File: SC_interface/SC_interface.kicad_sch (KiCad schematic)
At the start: 0 parts

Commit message: updated desgin doc, draw draft of the schematic
V1 circuit
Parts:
- added C1, C12: 0.47uf 400V, symbol Device:C_Small
- added C10, C11, C2, C5, C7: 0.1uf, symbol Device:C_Small
- added C3, C4, C6, C8, C9: 330uf 25V, symbol Device:C_Polarized_Small
- added D1: SMCJ6.0A, PCM_Diode_SMD_AKL:D_SMC, symbol PCM_Diode_TVS_AKL:SMCJ6.0A
- added D2, D3, D4, D5: 1N4148W, digikey-footprints:SOD-123, symbol dk_Diodes-Rectifiers-Single:1N4148W-7-F
- added F2: MF-MSMF110, MF-MSMF110:FUSER_MF-MSMF110, symbol MF-MSMF110:MF-MSMF110
- added J1: Input1, PCM_SparkFun-Connector:1x02, symbol Connector:Conn_Coaxial
- added J2: Output_BNC1, PCM_SparkFun-Connector:1x02, symbol Connector:Conn_Coaxial
- added Q1, Q2, Q3, Q4: LND150N8, PCM_Package_TO_SOT_SMD_AKL:SOT-89-3, symbol PCM_Transistor_MOSFET_AKL:LND150N8
- added R1: 90.9k, PCM_SparkFun-Resistor:R_0603_1608Metric, symbol PCM_SparkFun-Resistor:R_Small
- added R2: 9.09k, PCM_SparkFun-Resistor:R_0603_1608Metric, symbol PCM_SparkFun-Resistor:R_Small
- added R3: 909, PCM_SparkFun-Resistor:R_0603_1608Metric, symbol PCM_SparkFun-Resistor:R_Small
- added R4: 102, PCM_SparkFun-Resistor:R_0603_1608Metric, symbol PCM_SparkFun-Resistor:R_Small
- added R5: 100k, PCM_SparkFun-Resistor:R_0603_1608Metric, symbol PCM_SparkFun-Resistor:R_Small
- added SW1: Main Power, Button_Switch_SMD:Nidec_Copal_CAS-120A, symbol Switch:SW_DPDT_x2
- added SW2: SW_Select, PCM_SparkFun-Resistor:R_0603_1608Metric, symbol Switch:SW_Rotary_1x4_MP
- added U1: JCA0305D03, JCA0305D03:XPDCDCCONV, symbol JCA0305D03:JCA0305D03
- added U2: U2 OPA1656IDR, Package_SO:SOIC-8_3.9x4.9mm_P1.27mm, symbol Amplifier_Operational:OPA1656ID
- added U3: INA134UA, PCM_Package_SO_AKL:SO-8_3.9x4.9mm_P1.27mm, symbol PCM_Amplifier_Difference_AKL:INA134UA
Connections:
- new net: Q3.1 (G), Q3.2 (S), Q4.1 (G), Q4.2 (S)
- new net: C12.2, Q3.3 (D), R4.1, R5.2
- new net: Q1.1 (G), Q1.2 (S), Q2.1 (G), Q2.2 (S)
- new net: Q1.3 (D), SW2.5
- new net: C6.1, C7.1, SW1.2 (B), U1.14 (+VOUT)
- new net: R3.1, R4.2, SW2.4
- new net: R2.1, R3.2, SW2.3
- new net: C2.1, C3.1, D1.1 (K), F2.2, U1.22 (+VIN), U1.23 (+VIN2)
- new net: R1.1, R2.2, SW2.2
- new net: C1.2, R1.2, SW2.1
- new net: U2.7, U3.2 (IN-)
- new net: U2.1, U3.3 (IN+)
- new net: J2.1 (In), U3.5 (SENSE), U3.6 (OUT)
- new net: C4.2, C5.1, SW1.5 (B), U1.11 (-VOUT)
- new net: D2.A, D3.K, Q2.3 (D), U2.3 (+)
- new net: C12.1, J1.2 (Ext)
- new net: D4.A, D5.K, Q4.3 (D), U2.5 (+)
- new net: C1.1, J1.1 (In)
- new net +5V: F2.1
- new net +VDC: C11.1, C8.1, D2.K, D4.K, SW1.3 (C), U2.8 (V+), U3.7 (V+)
- new net -VDC: C10.1, C9.2, D3.A, D5.A, SW1.6 (C), U2.4 (V-), U3.4 (V-)
- new net GND: C10.2, C11.2, C4.1, C5.2, C6.2, C7.2, C8.2, C9.1, J2.2 (Ext), R5.1, U1.16 (COMMON2), U1.9 (COMMON), U3.1 (REF)
- new net GNDREF: C2.2, C3.2, D1.2 (A), U1.2 (-VIN), U1.3 (-VIN2)

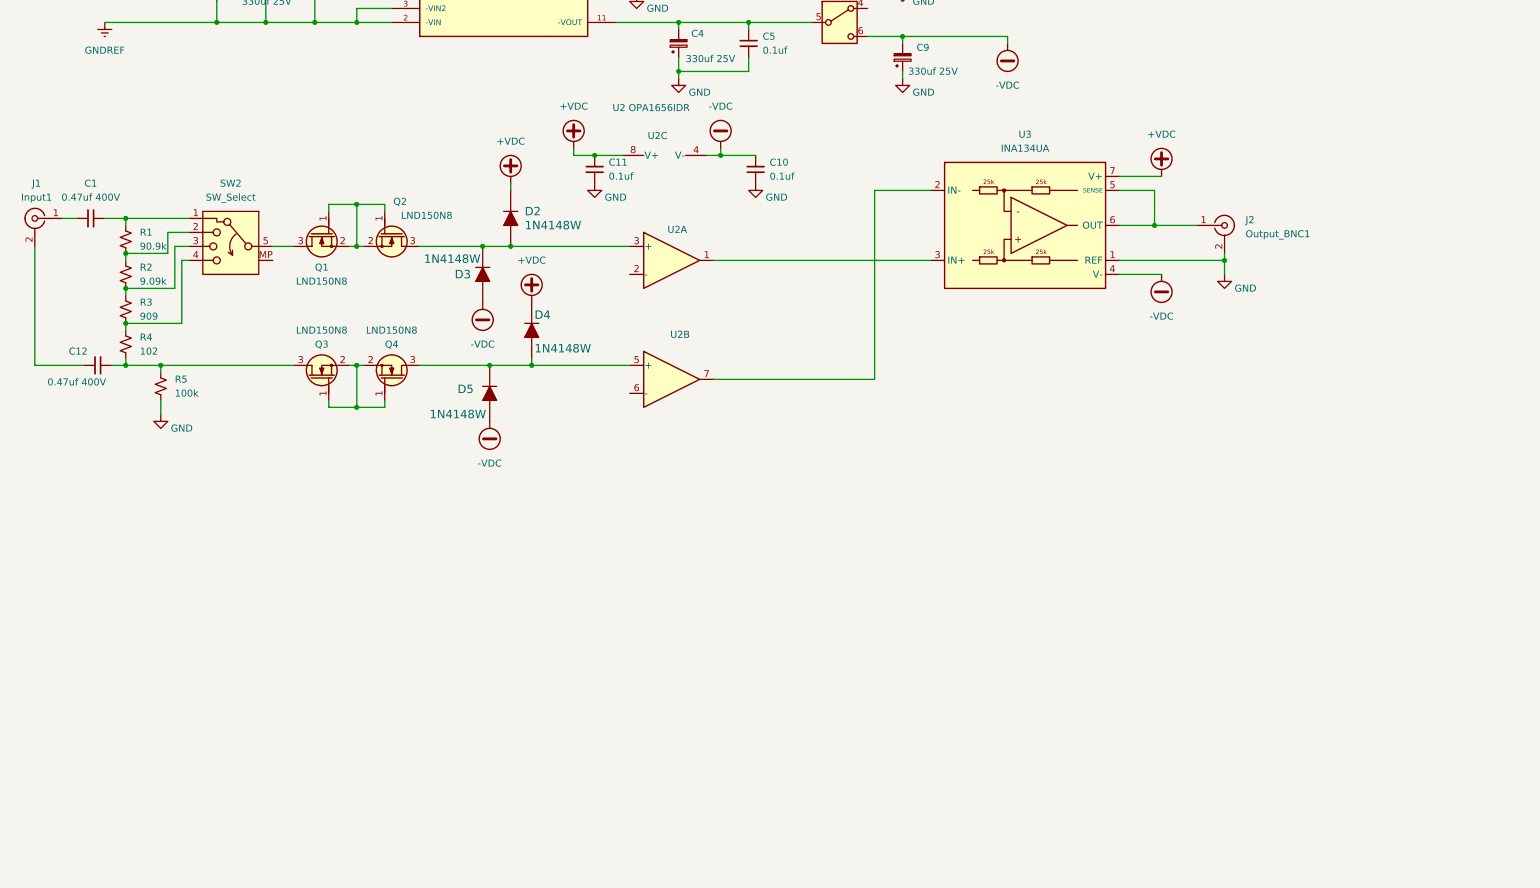
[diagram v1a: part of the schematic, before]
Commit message: completed Channel 1
completed two opamps
completed clamping network
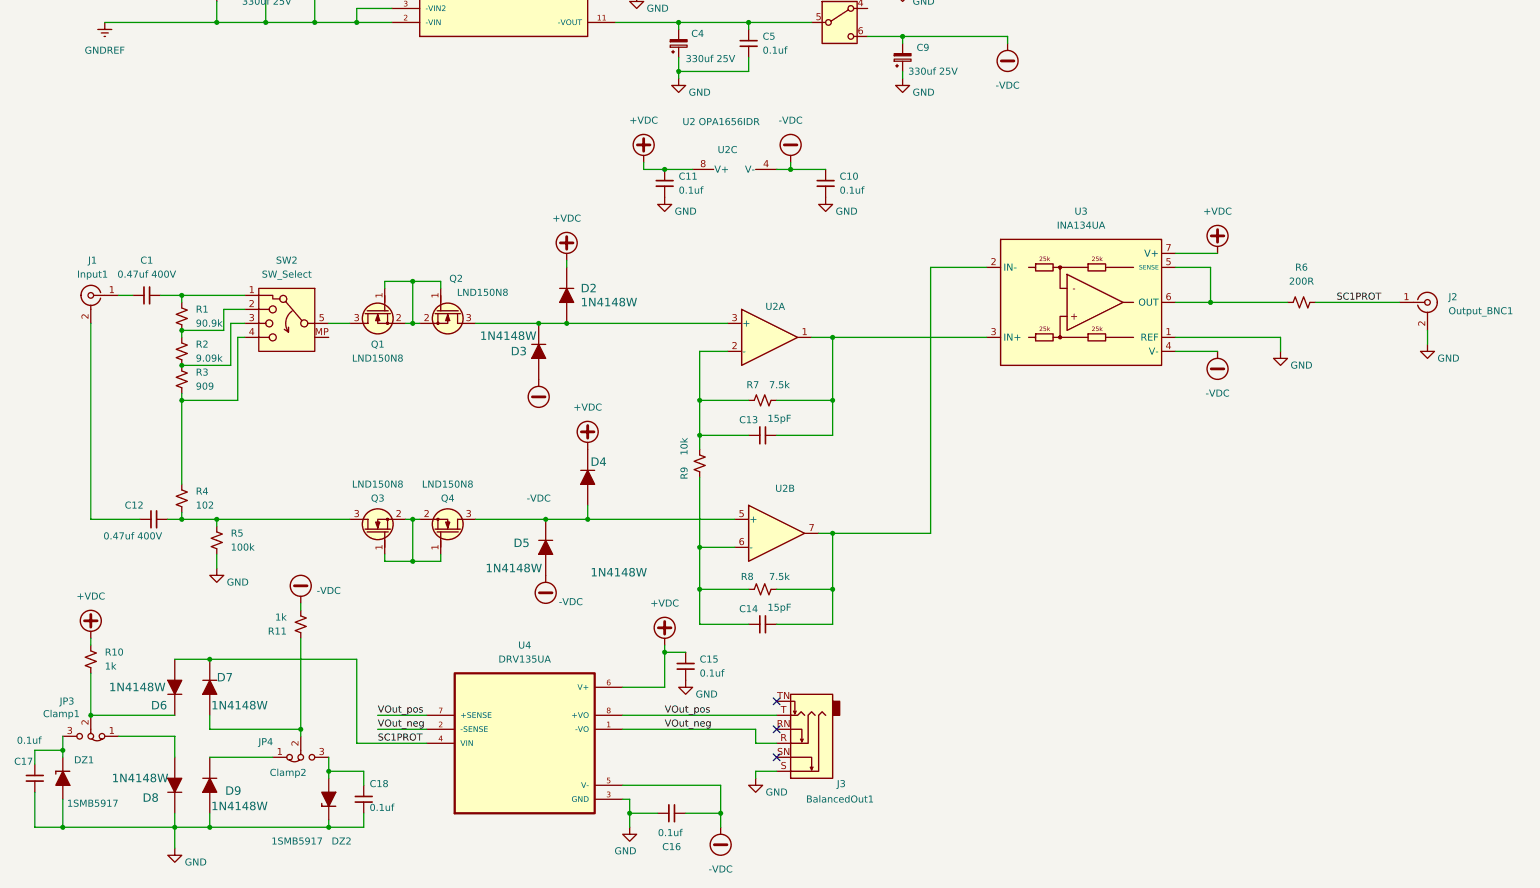
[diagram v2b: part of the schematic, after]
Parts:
- added C13, C14: 15pF, PCM_SparkFun-Resistor:R_0603_1608Metric, symbol Device:C_Small
- added C15, C16, C17, C18: 0.1uf, symbol Device:C_Small
- added D6, D7, D8, D9: 1N4148W, digikey-footprints:SOD-123, symbol dk_Diodes-Rectifiers-Single:1N4148W-7-F
- added DZ1, DZ2: 1SMB5917, PCM_Diode_SMD_AKL:D_SMB, symbol PCM_Diode_Zener_AKL:1SMB5917
- added J3: BalancedOut1, Connector_Audio:Jack_6.35mm_Neutrik_NMJ6HCD2_Horizontal, symbol Connector_Audio:NMJ6HCD2
- added JP3: Clamp1, Package_LCC:PLCC-84_29.3x29.3mm_P1.27mm, symbol Jumper:Jumper_3_Bridged12
- added JP4: Clamp2, Package_LCC:PLCC-84_29.3x29.3mm_P1.27mm, symbol Jumper:Jumper_3_Bridged12
- added R10, R11: 1k, PCM_SparkFun-Resistor:R_0603_1608Metric, symbol PCM_SparkFun-Resistor:R_Small
- added R6: 200R, PCM_SparkFun-Resistor:R_0603_1608Metric, symbol PCM_SparkFun-Resistor:R_Small
- added R7, R8: 7.5k, PCM_SparkFun-Resistor:R_0603_1608Metric, symbol PCM_SparkFun-Resistor:R_Small
- added R9: 10k, PCM_SparkFun-Resistor:R_0603_1608Metric, symbol PCM_SparkFun-Resistor:R_Small
- added U4: DRV135UA, DRV135UA:SOIC127P599X175-8N, symbol DRV135UA:DRV135UA
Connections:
- net +VDC: now also C15.1, R10.2, U4.6 (V+)
- net -VDC: now also C16.2, R11.1, U4.5 (V-)
- net GND: now also C15.2, C16.1, C17.1, C18.1, D8.K, D9.A, DZ1.2 (A), DZ2.1 (K), J3.S, U4.3 (GND)
- net at U2.7, U3.2 (IN-): now also C14.2, R8.2
- net at U2.1, U3.3 (IN+): now also C13.2, R7.2
- net at U3.5 (SENSE), U3.6 (OUT): now also R6.1; no longer J2.1 (In)
- net at U2.2 (-): now also C13.1, R7.1, R9.2
- net at U2.6 (-): now also C14.1, R8.1, R9.1
- new net: D8.A, JP3.1 (A)
- new net: C18.2, DZ2.2 (A), JP4.3 (B)
- new net: D6.K, JP3.2 (C), R10.1
- new net: C17.2, DZ1.1 (K), JP3.3 (B)
- new net: D9.K, JP4.1 (A)
- new net: D7.A, JP4.2 (C), R11.2
- new net SC1PROT: D6.A, D7.K, J2.1 (In), R6.2, U4.4 (VIN)
- new net VOut_neg: J3.R, U4.1 (-VO), U4.2 (-SENSE)
- new net VOut_pos: J3.T, U4.7 (+SENSE), U4.8 (+VO)
- no-connect marks 0 -> 3
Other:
- moved on the sheet: C1, C10, C11, C12, D2, D3, D4, D5, J1, J2, Q1, Q2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

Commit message: added channel 2
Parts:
- SW2: value SW_Select -> SW_Select1
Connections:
- net VOut_neg renamed VOut_neg1
- net VOut_pos renamed VOut_pos1
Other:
- added sheet Channel2 (Channel2.kicad_sch)
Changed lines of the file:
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@@
 		)
 	)
-	(label "VOut_pos"
+	(label "VOut_pos1"
 		(at 80.01 167.64 0)
 		(effects
@@
 		)
 	)
-	(label "VOut_pos"
+	(label "VOut_pos1"
 		(at 132.08 167.64 0)
 		(effects
@@
 		)
 	)
-	(label "VOut_neg"
+	(label "VOut_neg1"
 		(at 132.08 170.18 0)
 		(effects
@@
 		)
 	)
-	(label "VOut_neg"
+	(label "VOut_neg1"
 		(at 80.01 170.18 0)
 		(effects
@@
 			)
 		)
-		(property "Value" "SW_Select"
+		(property "Value" "SW_Select1"
 			(at 63.5 87.63 0)
 			(show_name no)
@@
 		(in_pos_files yes)
 		(dnp no)
-		(fields_autoplaced yes)
 		(property "Reference" "J1"
-			(at 28.2574 85.09 0)
+			(at 23.114 86.868 0)
 			(show_name no)
 			(do_not_autoplace no)
@@
 		)
 		(property "Value" "Input1"
-			(at 28.2574 87.63 0)
+			(at 21.59 90.932 0)
 			(show_name no)
 			(do_not_autoplace no)
@@
 				)
 			)
+		)
+	)
+	(sheet
+		(at 0 219.71)
+		(size 298.45 173.99)
+		(exclude_from_sim no)
+		(in_bom yes)
+		(on_board yes)
+		(dnp no)
+		(fields_autoplaced yes)
+		(stroke
+			(width 0.1524)
+			(type solid)
+		)
+		(fill
+			(color 0 0 0 0)
+		)
+		(property "Sheetname" "Channel2"
+			(at 0 218.9984 0)
+			(show_name no)
+			(do_not_autoplace no)
+			(effects
+				(font
+					(size 1.27 1.27)
+				)
+				(justify left bottom)
+			)
+		)
+		(property "Sheetfile" "Channel2.kicad_sch"
+			(at 0 394.2846 0)
+			(show_name no)
+			(do_not_autoplace no)
+			(effects
+				(font
+					(size 1.27 1.27)
+				)
+				(justify left top)
+			)
+		)
+		(instances
+			(project "SC_interface"
+				(path "/7297adbd-96ee-49f2-9956-85a279898d34"
+					(page "2")
+				)
+			)

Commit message: schemetic change and initial 3D rendering
Added master switch, some LED, Test Point.
Fixed all the footprint issues, passed ECE check
Initial 3D rendering the PCB update
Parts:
- removed C1, C12: 0.47uf 400V, symbol Device:C_Small
- removed C10, C11, C15, C16, C17, C18: 0.1uf, symbol Device:C_Small
- removed C13, C14: 15pF, PCM_SparkFun-Resistor:R_0603_1608Metric, symbol Device:C_Small
- removed C8, C9: 330uf 25V, symbol Device:C_Polarized_Small
- removed D2, D3, D4, D5, D6, D7, D8, D9: 1N4148W, digikey-footprints:SOD-123, symbol dk_Diodes-Rectifiers-Single:1N4148W-7-F
- removed DZ1, DZ2: 1SMB5917, PCM_Diode_SMD_AKL:D_SMB, symbol PCM_Diode_Zener_AKL:1SMB5917
- removed J1: Input1, PCM_SparkFun-Connector:1x02, symbol Connector:Conn_Coaxial
- removed J2: Output_BNC1, PCM_SparkFun-Connector:1x02, symbol Connector:Conn_Coaxial
- removed J3: BalancedOut1, Connector_Audio:Jack_6.35mm_Neutrik_NMJ6HCD2_Horizontal, symbol Connector_Audio:NMJ6HCD2
- removed JP3: Clamp1, Package_LCC:PLCC-84_29.3x29.3mm_P1.27mm, symbol Jumper:Jumper_3_Bridged12
- removed JP4: Clamp2, Package_LCC:PLCC-84_29.3x29.3mm_P1.27mm, symbol Jumper:Jumper_3_Bridged12
- removed Q1, Q2, Q3, Q4: LND150N8, PCM_Package_TO_SOT_SMD_AKL:SOT-89-3, symbol PCM_Transistor_MOSFET_AKL:LND150N8
- removed R1: 90.9k, PCM_SparkFun-Resistor:R_0603_1608Metric, symbol PCM_SparkFun-Resistor:R_Small
- removed R10, R11: 1k, PCM_SparkFun-Resistor:R_0603_1608Metric, symbol PCM_SparkFun-Resistor:R_Small
- removed R2: 9.09k, PCM_SparkFun-Resistor:R_0603_1608Metric, symbol PCM_SparkFun-Resistor:R_Small
- removed R3: 909, PCM_SparkFun-Resistor:R_0603_1608Metric, symbol PCM_SparkFun-Resistor:R_Small
- removed R4: 102, PCM_SparkFun-Resistor:R_0603_1608Metric, symbol PCM_SparkFun-Resistor:R_Small
- removed R5: 100k, PCM_SparkFun-Resistor:R_0603_1608Metric, symbol PCM_SparkFun-Resistor:R_Small
- removed R6: 200R, PCM_SparkFun-Resistor:R_0603_1608Metric, symbol PCM_SparkFun-Resistor:R_Small
- removed R7, R8: 7.5k, PCM_SparkFun-Resistor:R_0603_1608Metric, symbol PCM_SparkFun-Resistor:R_Small
- removed R9: 10k, PCM_SparkFun-Resistor:R_0603_1608Metric, symbol PCM_SparkFun-Resistor:R_Small
- removed SW2: SW_Select1, PCM_SparkFun-Resistor:R_0603_1608Metric, symbol Switch:SW_Rotary_1x4_MP
- removed U2: U2 OPA1656IDR, Package_SO:SOIC-8_3.9x4.9mm_P1.27mm, symbol Amplifier_Operational:OPA1656ID
- removed U3: INA134UA, PCM_Package_SO_AKL:SO-8_3.9x4.9mm_P1.27mm, symbol PCM_Amplifier_Difference_AKL:INA134UA
- removed U4: DRV135UA, DRV135UA:SOIC127P599X175-8N, symbol DRV135UA:DRV135UA
- added C107: 10nF 1kV, Capacitor_THT:C_Disc_D7.5mm_W5.0mm_P5.00mm, symbol Device:C_Small
- added D102: M_PWR, PCM_SparkFun-Resistor:R_0603_1608Metric, symbol Device:LED
- added D103: PWR_PS, PCM_SparkFun-Resistor:R_0603_1608Metric, symbol Device:LED
- added D104: PWR_NEG, PCM_SparkFun-Resistor:R_0603_1608Metric, symbol Device:LED
- added J101: 5V_PWR, Connector_PinHeader_2.54mm:PinHeader_1x02_P2.54mm_Vertical, symbol Connector:Conn_01x02_Pin
- added J102: J_chassis, Connector_Wire:SolderWire-1.5sqmm_1x01_D1.7mm_OD3mm, symbol Connector:Conn_01x01_Pin
- added R101: 470R, PCM_SparkFun-Resistor:R_0603_1608Metric, symbol PCM_SparkFun-Resistor:R_Small
- added R102, R103: 3K, PCM_SparkFun-Resistor:R_0603_1608Metric, symbol PCM_SparkFun-Resistor:R_Small
- added R104: 1M, 1W, Resistor_THT:R_Axial_DIN0207_L6.3mm_D2.5mm_P10.16mm_Horizontal, symbol PCM_SparkFun-Resistor:R_Small
- added SW102: Master SW, Connector_PinHeader_2.54mm:PinHeader_2x03_P2.54mm_Vertical, symbol Switch:SW_DPDT_x2
- added TP101: TP_POS, Connector_PinHeader_2.54mm:PinHeader_1x02_P2.54mm_Vertical, symbol Connector:TestPoint_2Pole
- added TP102: TP_NEG, Connector_PinHeader_2.54mm:PinHeader_1x02_P2.54mm_Vertical, symbol Connector:TestPoint_2Pole
- added TP103: TP_GND, Connector_PinHeader_2.54mm:PinHeader_1x02_P2.54mm_Vertical, symbol Connector:TestPoint_2Pole
- C101: renamed from C3; footprint (none) -> Capacitor_THT:CP_Radial_D8.0mm_P3.50mm
- C102: renamed from C2; footprint (none) -> Capacitor_SMD:C_0805_2012Metric_Pad1.18x1.45mm_HandSolder
- C103: renamed from C6; footprint (none) -> Capacitor_THT:CP_Radial_D8.0mm_P3.50mm
- C104: renamed from C4; footprint (none) -> Capacitor_THT:CP_Radial_D8.0mm_P3.50mm
- C105: renamed from C7; footprint (none) -> Capacitor_SMD:C_0805_2012Metric_Pad1.18x1.45mm_HandSolder
- C106: renamed from C5; footprint (none) -> Capacitor_SMD:C_0805_2012Metric_Pad1.18x1.45mm_HandSolder
- D101: renamed from D1; footprint PCM_Diode_SMD_AKL:D_SMC -> Diode_SMD:D_SMC_Handsoldering
- F101: renamed from F2; footprint MF-MSMF110:FUSER_MF-MSMF110 -> Fuse:Fuse_1812_4532Metric_Pad1.30x3.40mm_HandSolder
- SW101: renamed from SW1; footprint Button_Switch_SMD:Nidec_Copal_CAS-120A -> Connector_PinHeader_2.54mm:PinHeader_2x03_P2.54mm_Vertical
- renumbered U1 to U101
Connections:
- net +VDC: now also R102.1, TP101.1, TP101.2
- net -VDC: now also R103.1, TP102.1, TP102.2
- net GND: now also C107.2, D103.1 (K), D104.2 (A), R104.2, TP103.1, TP103.2
- net GNDREF: now also D102.1 (K), J101.2 (Pin_2)
- net at C101.1, C102.1, D101.1 (K)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: now also R101.1
- net +5V: no longer names the net of F101.1
- net +5V: now also SW102.3 (C), SW102.6 (C)
- new net: D104.1 (K), R103.2
- new net: D102.2 (A), R101.2
- new net: C107.1, J102.1 (Pin_1), R104.1
- new net: D103.2 (A), R102.2
- new net 5V_in: J101.1 (Pin_1), SW102.2 (B), SW102.5 (B)
- no-connect marks 3 -> 4
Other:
- removed sheet Channel2
- added sheet Input_ChannelL (InputChannel.kicad_sch)
- added sheet Input_ChannelR (InputChannel.kicad_sch)
- note added: "Chassis Ground Lug"
- note added: "Main Power Supply"
- note added: "Sheet 2 & 3 have Input Channel L & R"
- moved on the sheet: C101, C102, C103, C104, C105, C106, D101, F101, SW101A, SW101B, U101
